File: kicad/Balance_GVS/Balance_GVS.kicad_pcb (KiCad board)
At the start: 2 copper layers, 110 parts, among them J1 Conn_01x02_Pin, J2 USB_C_Receptacle, J3 Conn_01x02_Pin, J4 Conn_01x02_Pin, J5 Conn_01x02_Pin, K1 AQY210S, Q3 2N3904, Q4 2N3904, SW2 EVQ-P7A01P, SW3 SW_Push, SW4 SW_Push, SW5 SW_Push, SW6 SW_Push, SW7 SS-12D00-G 4 E, U1 ESP32-WROOM-32E, U10 INA219BxD, U11 LT1013DIP, U12 LT1013DIP, U3 OPA4313IPWR, U4 INA303A1IPW, U5 TPS7A4901DGNT, U7 MT3608, U8 TP4056, U9 MCP4725xxx-xCH

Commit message: partial non-battery PCB now moved
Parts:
- moved R23 219.6 mm to (265.0, 52.0), turned to -90 degrees
- moved R25 212.7 mm to (254.5, 52.0), turned to 90 degrees
- moved R26 207.1 mm to (249.5, 57.5), turned to 90 degrees
- moved R27 206.3 mm to (258.0, 49.5)
- moved R24 206.3 mm to (256.5, 69.0), turned to -90 degrees
- moved R43 205.9 mm to (250.5, 47.0), turned to -90 degrees
- moved R22 201.5 mm to (252.5, 66.0), turned to 90 degrees
- moved R1 201.2 mm to (252.5, 61.0), turned to -90 degrees
- moved R28 200.8 mm to (254.0, 57.0), turned to 90 degrees
- moved C15 193.1 mm to (265.2, 55.8), turned to 90 degrees
- moved R48 187.9 mm to (248.5, 69.0), turned to 90 degrees
- moved R45 185.2 mm to (235.5, 69.0), turned to 90 degrees
- moved R47 178.0 mm to (239.0, 69.0), turned to 90 degrees
- moved C24 176.5 mm to (247.5, 47.0), turned to 90 degrees
- moved C16 176.5 mm to (261.5, 64.5), turned to -90 degrees
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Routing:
- net 24V: track 0.00 -> 61.8 mm, vias 0 -> 2
- net /HowlandPump/3IN-: track 0.00 -> 46.4 mm, vias 0 -> 2
- net Electrode+: track 0.00 -> 34.2 mm, vias 0 -> 2
- net +3.3V: track 0.00 -> 32.5 mm
- net /Processor/POT_ADC: track 0.00 -> 25.7 mm
- net /HowlandPump/12V: track 0.00 -> 22.0 mm
- net /Processor/EN: track 0.00 -> 21.9 mm
- net /Processor/Button1: track 0.00 -> 20.5 mm
- net /Processor/Switch1: track 0.00 -> 20.2 mm, vias 0 -> 2
- net /Processor/SCL2: track 0.00 -> 19.2 mm, vias 0 -> 2
- net /Processor/SDA2: track 0.00 -> 18.6 mm
- net /Processor/SCL1: track 0.00 -> 16.8 mm, vias 0 -> 2
- net Net-(Q4-B): track 0.00 -> 16.5 mm
- net /Processor/SDA1: track 0.00 -> 15.8 mm
- net Net-(Q3-B): track 0.00 -> 15.4 mm
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
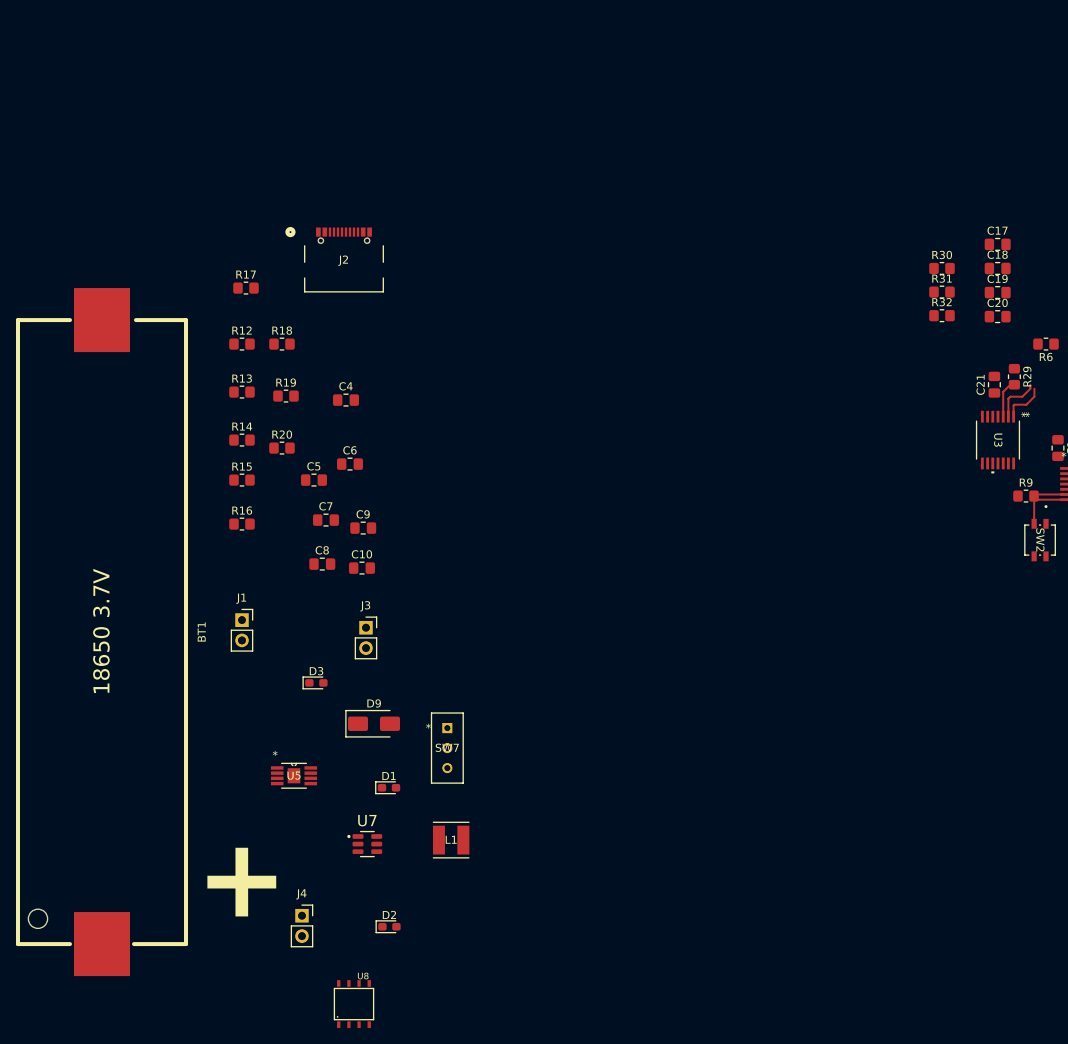
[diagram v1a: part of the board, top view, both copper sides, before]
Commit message: now without battery components in pcb
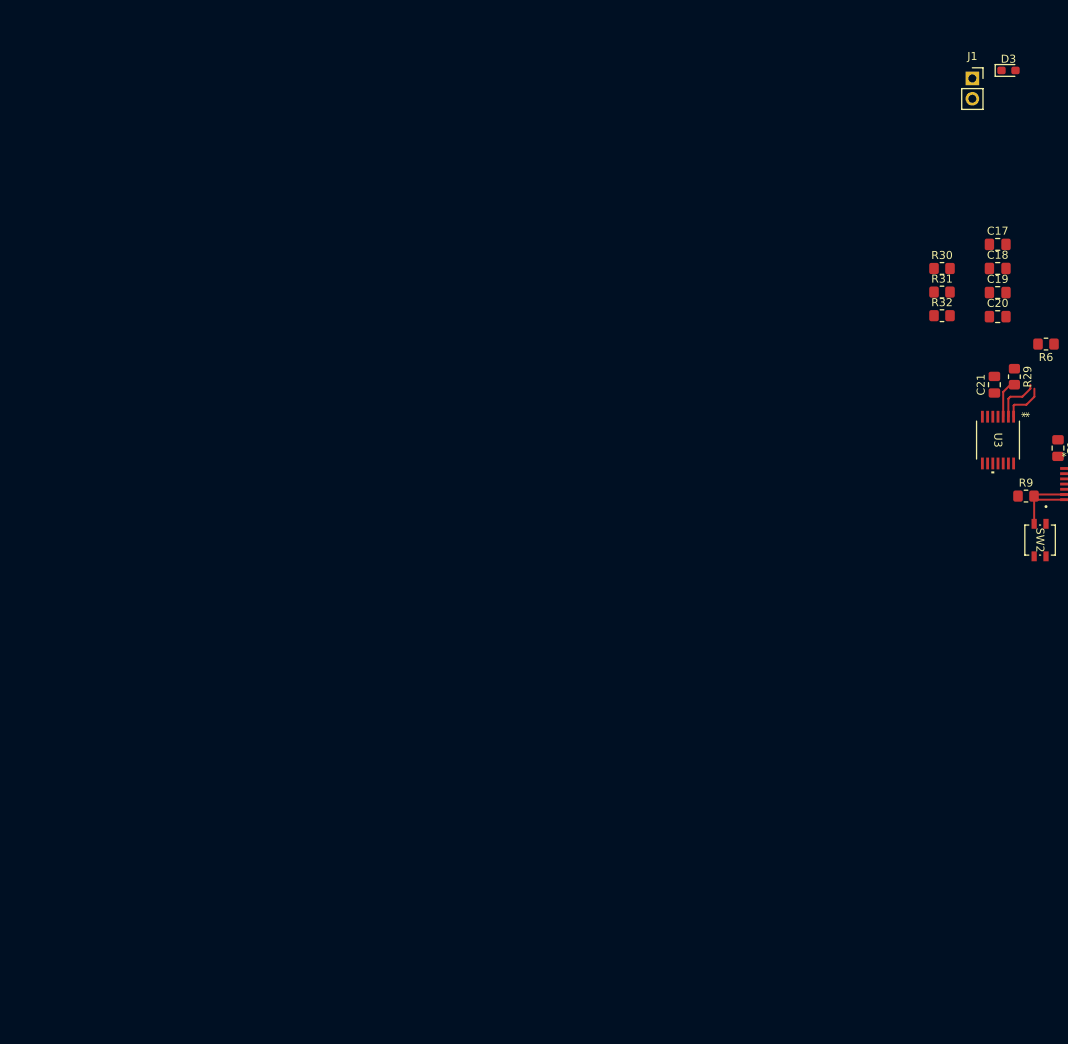
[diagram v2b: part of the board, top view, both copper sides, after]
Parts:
- removed BT1: BK-18650-PC2, FreddyBattery:BH-18650-B1BA002
- removed C10: 2.2µF, Capacitor_SMD:C_0805_2012Metric_Pad1.18x1.45mm_HandSolder
- removed C4, C5, C6, C8, C9: 10µF, Capacitor_SMD:C_0805_2012Metric_Pad1.18x1.45mm_HandSolder
- removed C7: 10nF, Capacitor_SMD:C_0805_2012Metric_Pad1.18x1.45mm_HandSolder
- removed D1, D2: LED_Small, LED_SMD:LED_0603_1608Metric_Pad1.05x0.95mm_HandSolder
- removed D9: SS14, Diode_SMD:D_SMA
- removed J2: USB_C_Receptacle, USB4105_GF_A:USB4105_GCT
- removed J3, J4: Conn_01x02_Pin, Connector_PinSocket_2.54mm:PinSocket_1x02_P2.54mm_Vertical
- removed L1: 4.7µH, SRN4018_4R7M:IND_BOURNS_SRN4018
- removed R12: 191k, Resistor_SMD:R_0805_2012Metric_Pad1.20x1.40mm_HandSolder
- removed R13, R20: 10k, Resistor_SMD:R_0805_2012Metric_Pad1.20x1.40mm_HandSolder
- removed R14: 2.4k, Resistor_SMD:R_0805_2012Metric_Pad1.20x1.40mm_HandSolder
- removed R15, R16: 1k, Resistor_SMD:R_0805_2012Metric_Pad1.20x1.40mm_HandSolder
- removed R17, R18: 5.1k, Resistor_SMD:R_0805_2012Metric_Pad1.20x1.40mm_HandSolder
- removed R19: 412k, Resistor_SMD:R_0805_2012Metric_Pad1.20x1.40mm_HandSolder
- removed SW7: SS-12D00-G 4 E, ul_SS-12D00-G-4-E:1P2T_SS-12D00_CNK
- removed U5: TPS7A4901DGNT, TPS7A4901DGNT _footprints:DGN8_1P89X1P57
- removed U7: MT3608, MT3608:SOT95P280X145-6N
- removed U8: TP4056, TP4056:SOT23-8
- moved D3 115.5 mm to (149.8, 65.3)
- moved J1 113.7 mm to (145.3, 66.3)

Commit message: connected non-battery PCB, with DRC errors
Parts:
- moved R31 122.1 mm to (258.4, 128.0)
- moved R30 119.6 mm to (254.4, 129.7)
- moved C19 113.3 mm to (257.0, 125.5)
- moved R32 110.0 mm to (249.8, 115.1), turned to -90 degrees
- moved C17 109.7 mm to (250.3, 127.7), turned to 180 degrees
- moved C21 108.1 mm to (253.9, 126.5), turned to -90 degrees
- moved C18 107.9 mm to (250.4, 125.2)
- moved C20 106.0 mm to (252.9, 114.0)
- moved U3 105.6 mm to (253.8, 119.6), turned to 90 degrees
- moved R29 103.9 mm to (250.9, 130.7)
- moved D3 98.9 mm to (233.2, 118.5), turned to -90 degrees
- moved R9 95.1 mm to (246.9, 125.1), turned to 90 degrees
- moved J1 91.6 mm to (230.2, 100.7), turned to 90 degrees
- moved SW2 87.1 mm to (240.9, 125.2), turned to 180 degrees
- moved U4 85.4 mm to (245.4, 117.2), turned to 90 degrees
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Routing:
- net 1.65V: track 0.00 -> 43.2 mm, vias 0 -> 4
- net Battery_Voltage: track 4.77 -> 41.7 mm
- net /HowlandPump/2IN+: track 3.08 -> 21.5 mm
- net /Safety/VREF: track 0.00 -> 17.1 mm, vias 0 -> 2
- net Net-(D3-K): track 8.86 -> 24.7 mm
- net /Safety/LIMIT2: track 4.45 -> 17.5 mm
- net /Safety/INP: track 4.44 -> 17.4 mm
- net /HowlandPump/3IN-: track 46.4 -> 36.1 mm
- net 24V: track 61.8 -> 51.5 mm
- net /Safety/0.825V: track 0.00 -> 9.69 mm
- net Electrode+: track 34.2 -> 24.8 mm
- net /Safety/2.475V: track 4.87 -> 12.9 mm
- net +3.3V: track 32.5 -> 35.5 mm
- net Net-(D3-A): track 0.00 -> 2.62 mm
- net /Safety/LIMIT1: track 11.5 -> 13.5 mm, vias 0 -> 2
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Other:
- board outline added: 30 x 100 mm

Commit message: Add shit ton to schematic
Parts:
- added C26: 10nF, Capacitor_SMD:C_0805_2012Metric_Pad1.18x1.45mm_HandSolder, F.Cu at (183.6, 95.2)
- added D10: BAS40, BAS40:P200_SOT-23, F.Cu at (171.3, 77.6)
- added D11: BAS40, BAS40:P200_SOT-23, F.Cu at (171.3, 82.1)
- added D12: BAS40, BAS40:P200_SOT-23, F.Cu at (171.3, 86.5)
- added D13: CMJ3500, Diode_SMD:D_SOD-123F, F.Cu at (182.2, 73.7)
- added D14: CMJ3500, Diode_SMD:D_SOD-123F, F.Cu at (182.2, 77.0)
- added D15: CMJ3500, Diode_SMD:D_SOD-123F, F.Cu at (182.2, 80.4)
- added D4: BAS40, BAS40:P200_SOT-23, F.Cu at (171.3, 73.2)
- added J10: I2C Header 2, Connector_PinSocket_2.54mm:PinSocket_1x02_P2.54mm_Vertical, F.Cu at (176.9, 96.0)
- added J6: Conn_01x03_Pin, Connector_PinHeader_2.54mm:PinHeader_1x03_P2.54mm_Vertical, F.Cu at (181.8, 84.3)
- added J7: Conn_01x03_Pin, Connector_PinHeader_2.54mm:PinHeader_1x03_P2.54mm_Vertical, F.Cu at (186.4, 84.3)
- added J8: Conn_01x05_Pin, Connector_PinSocket_2.54mm:PinSocket_1x05_P2.54mm_Vertical, F.Cu at (177.2, 74.3)
- added J9: I2C Header 1, Connector_PinSocket_2.54mm:PinSocket_1x02_P2.54mm_Vertical, F.Cu at (172.3, 96.0)
- added R52: 10k, Resistor_SMD:R_0805_2012Metric_Pad1.20x1.40mm_HandSolder, F.Cu at (183.6, 98.2)
- R23: value 10K -> 33
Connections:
- K1 pad 4: Electrode- -> Safety+
- R23 pad 1: INA219_IN+ -> Safety-
- R23 pad 2: INA219_IN- -> Current_Sense-
- R39 pad 2: Safety- -> Current_Sense-
- U10 pad 7: INA219_IN- -> Current_Sense-
- U10 pad 8: INA219_IN+ -> Safety-
- U11 pad 3: DAC_OUT -> Net-(U11-1IN_+)
- U12 pad 7: Safety- -> Current_Sense-
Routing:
- net Current_Sense-: track 0.00 -> 6.70 mm
- net INA219_IN+: track 3.53 -> 0.00 mm
- net INA219_IN-: track 2.85 -> 0.00 mm

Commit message: Youssef's change
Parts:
- moved D15 107.7 mm to (280.0, 125.5)
- moved D14 105.9 mm to (279.5, 119.0)
- moved D13 105.0 mm to (279.6, 113.0)
- moved J8 101.0 mm to (278.0, 68.9)
- moved J6 99.5 mm to (280.0, 100.5)
- moved J10 98.3 mm to (272.0, 120.7)
- moved D10 96.2 mm to (267.0, 88.1), turned to 90 degrees
- moved J9 94.7 mm to (264.4, 118.0)
- moved J7 92.2 mm to (278.5, 88.0)
- moved C26 91.3 mm to (274.5, 104.5)
- moved R52 89.5 mm to (272.0, 112.0)
- moved D11 88.6 mm to (259.8, 88.0)
- moved D4 88.3 mm to (259.3, 81.5)
- moved D12 86.7 mm to (257.6, 95.7)
- moved J5 21.4 mm to (276.0, 53.5)
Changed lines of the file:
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@@
 			(net "Net-(Q3-B)")
 			(pinfunction "*ALERT2_11")
-			(pintype "output")
+			(pintype "open_collector")
 		)
 		(pad "12" smd rect
@@
 			(net "Net-(Q3-B)")
 			(pinfunction "*ALERT1_12")
-			(pintype "output")
+			(pintype "open_collector")
 		)
 		(pad "13" smd rect
@@
 	(footprint "BAS40:P200_SOT-23"
 		(layer "F.Cu")
-		(at 171.345 77.645)
+		(at 266.97 88.1 90)
 		(descr "SOT, 3 Pin (https://www.jedec.org/system/files/docs/to-236h.pdf variant AB), generated with kicad-footprint-generator ipc_gullwing_generator.py")
 		(tags "SOT TO_SOT_SMD")
 		(property "Reference" "D10"
-			(at 0.5 -1.25 0)
+			(at 1.2 -1.47 90)
 			(layer "F.SilkS")
 			(effects
@@
 		)
 		(property "Value" "BAS40"
-			(at 1 3.43 0)
+			(at 1 3.43 90)
 			(layer "F.Fab")
 			(effects
@@
 		)
 		(property "Datasheet" "https://diotec.com/de/produktliste/D.html"
-			(at 0 0 0)
+			(at 0 0 90)
 			(layer "F.Fab")
 			(hide yes)
@@
 		)
 		(property "Description" "Diode with NC pin"
-			(at 0 0 0)
+			(at 0 0 90)
 			(layer "F.Fab")
 			(hide yes)
@@
 		(fp_line
 			(start 1.1 -0.62)
-			(end -0.575 -0.62)
+			(end 1.75 -0.62)
 			(stroke
 				(width 0.12)
@@
 		(fp_line
 			(start 1.1 -0.62)
-			(end 1.75 -0.62)
+			(end -0.575 -0.62)
 			(stroke
 				(width 0.12)
@@
 		(fp_line
 			(start 1.1 2.68)
-			(end 0.45 2.68)
+			(end 1.75 2.68)
 			(stroke
 				(width 0.12)
@@
 		(fp_line
 			(start 1.1 2.68)
-			(end 1.75 2.68)
+			(end 0.45 2.68)
 			(stroke
 				(width 0.12)
@@
 		)
 		(fp_line
-			(start -0.82 -0.67)
-			(end -0.82 2.73)
+			(start 3.02 -0.67)
+			(end -0.82 -0.67)
 			(stroke
 				(width 0.05)
@@
 		)
 		(fp_line
-			(start -0.82 2.73)
-			(end 3.02 2.73)
+			(start -0.82 -0.67)
+			(end -0.82 2.73)
 			(stroke
 				(width 0.05)
@@
 		)
 		(fp_line
-			(start 3.02 -0.67)
-			(end -0.82 -0.67)
+			(start 3.02 2.73)
+			(end 3.02 -0.67)
 			(stroke
 				(width 0.05)
@@
 		)
 		(fp_line
-			(start 3.02 2.73)
-			(end 3.02 -0.67)
+			(start -0.82 2.73)
+			(end 3.02 2.73)
 			(stroke
 				(width 0.05)
@@
 		)
 		(fp_line
-			(start 0.45 -0.145)
-			(end 0.775 -0.47)
+			(start 1.75 -0.47)
+			(end 1.75 2.53)
 			(stroke
 				(width 0.1)
@@
 		)
 		(fp_line
-			(start 0.45 2.53)
-			(end 0.45 -0.145)
+			(start 0.775 -0.47)
+			(end 1.75 -0.47)
 			(stroke
 				(width 0.1)
@@
 		)
 		(fp_line
-			(start 0.775 -0.47)
-			(end 1.75 -0.47)
+			(start 0.45 -0.145)
+			(end 0.775 -0.47)
 			(stroke
 				(width 0.1)
@@
 		)
 		(fp_line
-			(start 1.75 -0.47)
-			(end 1.75 2.53)
+			(start 1.75 2.53)
+			(end 0.45 2.53)
 			(stroke
 				(width 0.1)
@@
 		)
 		(fp_line
-			(start 1.75 2.53)
-			(end 0.45 2.53)
+			(start 0.45 2.53)
+			(end 0.45 -0.145)
 			(stroke
 				(width 0.1)
@@
 		)
 		(fp_text user "${REFERENCE}"
-			(at 0.5 -1.25 0)
+			(at 1.2 -1.47 90)
 			(layer "F.Fab")
 			(effects
@@
 		)
 		(pad "1" smd roundrect
-			(at 0 0)
+			(at 0 0 90)
 			(size 1 0.6)
 			(layers "F.Cu" "F.Mask" "F.Paste")
@@
 		)
 		(pad "2" smd roundrect
-			(at 0 2.06)
+			(at 0 2.06 90)
 			(size 1 0.6)
 			(layers "F.Cu" "F.Mask" "F.Paste")
@@
 		)
 		(pad "3" smd roundrect
-			(at 2.2 1.03)
+			(at 2.2 1.03 90)
 			(size 1 0.6)
 			(layers "F.Cu" "F.Mask" "F.Paste")
@@
 		)
 		(embedded_fonts no)
-		(model "${KICAD6_3DMODEL_DIR}/Package_TO_SOT_SMD.3dshapes/SOT-23.wrl"
+		(model "${KICAD10_3DMODEL_DIR}/Package_TO_SOT_SMD.3dshapes/SOT-23.step"
 			(hide yes)
 			(offset
@@
 	(footprint "BAS40:P200_SOT-23"
 		(layer "F.Cu")
-		(at 171.345 73.195)
+		(at 259.3 81.47)
 		(descr "SOT, 3 Pin (https://www.jedec.org/system/files/docs/to-236h.pdf variant AB), generated with kicad-footprint-generator ipc_gullwing_generator.py")
 		(tags "SOT TO_SOT_SMD")
@@
 		)
 		(embedded_fonts no)
-		(model "${KICAD6_3DMODEL_DIR}/Package_TO_SOT_SMD.3dshapes/SOT-23.wrl"
+		(model "${KICAD10_3DMODEL_DIR}/Package_TO_SOT_SMD.3dshapes/SOT-23.step"
 			(hide yes)
 			(offset
@@
 	(footprint "BAS40:P200_SOT-23"
 		(layer "F.Cu")
-		(at 171.345 86.545)
+		(at 257.57 95.7)
 		(descr "SOT, 3 Pin (https://www.jedec.org/system/files/docs/to-236h.pdf variant AB), generated with kicad-footprint-generator ipc_gullwing_generator.py")
 		(tags "SOT TO_SOT_SMD")
@@
 		)
 		(embedded_fonts no)
-		(model "${KICAD6_3DMODEL_DIR}/Package_TO_SOT_SMD.3dshapes/SOT-23.wrl"
+		(model "${KICAD10_3DMODEL_DIR}/Package_TO_SOT_SMD.3dshapes/SOT-23.step"
 			(hide yes)
 			(offset
@@
 	(footprint "Diode_SMD:D_SOD-123F"
 		(layer "F.Cu")
-		(at 182.25 73.675)
+		(at 279.6 113)
 		(descr "D_SOD-123F")
 		(tags "D_SOD-123F")
@@
 	(footprint "Connector_PinSocket_2.54mm:PinSocket_1x02_P2.54mm_Vertical"
 		(layer "F.Cu")
-		(at 176.885 96.015)
+		(at 272 120.73)
 		(descr "Through hole straight socket strip, 1x02, 2.54mm pitch, single row (from Kicad 4.0.7), script generated")
 		(tags "Through hole socket strip THT 1x02 2.54mm single row")
@@
 	(footprint "Connector_PinSocket_2.54mm:PinSocket_1x02_P2.54mm_Vertical"
 		(layer "F.Cu")
-		(at 172.295 96.015)
+		(at 264.41 117.96)
 		(descr "Through hole straight socket strip, 1x02, 2.54mm pitch, single row (from Kicad 4.0.7), script generated")
 		(tags "Through hole socket strip THT 1x02 2.54mm single row")
@@
 	(footprint "Connector_PinHeader_2.54mm:PinHeader_1x03_P2.54mm_Vertical"
 		(layer "F.Cu")
-		(at 186.365 84.345)
+		(at 278.5 88)
 		(descr "Through hole straight pin header, 1x03, 2.54mm pitch, single row")
 		(tags "Through hole pin header THT 1x03 2.54mm single row")
@@
 	(footprint "BAS40:P200_SOT-23"
 		(layer "F.Cu")
-		(at 171.345 82.095)
+		(at 259.8 87.97)
 		(descr "SOT, 3 Pin (https://www.jedec.org/system/files/docs/to-236h.pdf variant AB), generated with kicad-footprint-generator ipc_gullwing_generator.py")
 		(tags "SOT TO_SOT_SMD")
@@
 		)
 		(embedded_fonts no)
-		(model "${KICAD6_3DMODEL_DIR}/Package_TO_SOT_SMD.3dshapes/SOT-23.wrl"
+		(model "${KICAD10_3DMODEL_DIR}/Package_TO_SOT_SMD.3dshapes/SOT-23.step"
 			(hide yes)
 			(offset
@@
 	(footprint "Connector_PinSocket_2.54mm:PinSocket_1x05_P2.54mm_Vertical"
 		(layer "F.Cu")
-		(at 177.185 74.295)
+		(at 278 68.88)
 		(descr "Through hole straight socket strip, 1x05, 2.54mm pitch, single row (from Kicad 4.0.7), script generated")
 		(tags "Through hole socket strip THT 1x05 2.54mm single row")
@@
 		)
 		(property "Value" "Conn_01x05_Pin"
-			(at 0 12.93 0)
+			(at 11.5 48.93 0)
 			(layer "F.Fab")
 			(effects
@@
 	(footprint "Connector_PinSocket_2.54mm:PinSocket_1x02_P2.54mm_Vertical"
 		(layer "F.Cu")
-		(at 268.5 73.5)
+		(at 276 53.5)
 		(descr "Through hole straight socket strip, 1x02, 2.54mm pitch, single row (from Kicad 4.0.7), script generated")
 		(tags "Through hole socket strip THT 1x02 2.54mm single row")
@@
 	(footprint "Diode_SMD:D_SOD-123F"
 		(layer "F.Cu")
-		(at 182.25 77.025)
+		(at 279.5 119)
 		(descr "D_SOD-123F")
 		(tags "D_SOD-123F")
@@
 	(footprint "Resistor_SMD:R_0805_2012Metric_Pad1.20x1.40mm_HandSolder"
 		(layer "F.Cu")
-		(at 183.555 98.205)
+		(at 272 112)
 		(descr "Resistor SMD 0805 (2012 Metric), square (rectangular) end terminal, IPC-7351 nominal with elongated pad for handsoldering. (Body size source: IPC-SM-782 page 72, https://www.pcb-3d.com/wordpress/wp-content/uploads/ipc-sm-782a_amendment_1_and_2.pdf)")
 		(tags "resistor handsolder")
@@
 	(footprint "Capacitor_SMD:C_0805_2012Metric_Pad1.18x1.45mm_HandSolder"
 		(layer "F.Cu")
-		(at 183.585 95.225)
+		(at 274.4625 104.5)
 		(descr "Capacitor SMD 0805 (2012 Metric), square (rectangular) end terminal, IPC-7351 nominal with elongated pad for handsoldering. (Body size source: IPC-SM-782 page 76, https://www.pcb-3d.com/wordpress/wp-content/uploads/ipc-sm-782a_amendment_1_and_2.pdf, https://docs.google.com/spreadsheets/d/1BsfQQcO9C6DZCsRaXUlFlo91Tg2WpOkGARC1WS5S8t0/edit?usp=sharing)")
 		(tags "capacitor handsolder")
@@
 	(footprint "Connector_PinHeader_2.54mm:PinHeader_1x03_P2.54mm_Vertical"
 		(layer "F.Cu")
-		(at 181.775 84.345)
+		(at 280 100.46)
 		(descr "Through hole straight pin header, 1x03, 2.54mm pitch, single row")
 		(tags "Through hole pin header THT 1x03 2.54mm single row")
@@
 	(footprint "Diode_SMD:D_SOD-123F"
 		(layer "F.Cu")
-		(at 182.25 80.375)
+		(at 279.975 125.53)
 		(descr "D_SOD-123F")
 		(tags "D_SOD-123F")
@@
 	)
 	(segment
+		(start 239.76 141.5)
+		(end 240.53 142.27)
+		(width 0.25)
+		(layer "F.Cu")
+		(net "Current_Sense-")
+	)
+	(segment
+		(start 262.225 53.185)
+		(end 264.815 53.185)
+		(width 0.2)
+		(layer "F.Cu")
+		(net "Current_Sense-")
+	)
+	(segment
+		(start 264.815 53.185)
+		(end 265 53)
+		(width 0.2)
+		(layer "F.Cu")
+		(net "Current_Sense-")
+	)
+	(segment
+		(start 237 141.5)
+		(end 239.76 141.5)
+		(width 0.25)
+		(layer "F.Cu")
+		(net "Current_Sense-")
+	)
+	(segment
 		(start 248 57.5)
 		(end 248 60.5)
@@
 		(net "Net-(U11-2OUT)")
 	)
-	(segment
-		(start 239.76 141.5)
-		(end 240.53 142.27)
-		(width 0.25)
-		(layer "F.Cu")
-		(net "Current_Sense-")
-	)
-	(segment
-		(start 262.225 53.185)
-		(end 264.815 53.185)
-		(width 0.2)
-		(layer "F.Cu")
-		(net "Current_Sense-")
-	)
-	(segment
-		(start 264.815 53.185)
-		(end 265 53)
-		(width 0.2)
-		(layer "F.Cu")
-		(net "Current_Sense-")
-	)
-	(segment
-		(start 237 141.5)
-		(end 239.76 141.5)
-		(width 0.25)
-		(layer "F.Cu")
-		(net "Current_Sense-")
-	)
 	(embedded_fonts no)

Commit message: adding CLDs in progress
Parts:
- moved J9 80.5 mm to (184.0, 121.5)
- moved J10 80.5 mm to (191.6, 124.3)
- moved J8 73.2 mm to (217.0, 109.4)
- moved D15 44.5 mm to (264.0, 84.0)
- moved D14 41.6 mm to (257.0, 84.0), turned to 180 degrees
- moved J6 35.1 mm to (249.0, 84.0)
- moved R52 33.8 mm to (276.5, 145.5)
- moved C26 30.8 mm to (267.5, 134.5)
- moved D13 30.4 mm to (255.1, 95.0)
- moved J7 16.0 mm to (265.0, 96.5), turned to 180 degrees
- moved D11 12.9 mm to (251.1, 97.6), turned to 180 degrees
- moved D4 10.3 mm to (255.4, 91.0), turned to 90 degrees
- moved D10 10.2 mm to (261.1, 96.5), turned to 180 degrees
- moved D12 6.84 mm to (253.9, 101.5), turned to 90 degrees
- moved R7 2.03 mm to (265.4, 129.0)
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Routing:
- net Net-(D10-A): track 0.00 -> 13.6 mm
- net Net-(D10-C): track 0.00 -> 13.5 mm
- net Net-(D11-A): track 0.00 -> 11.6 mm
- net /HowlandPump/1IN-: track 11.7 -> 0.21 mm
- net Net-(D11-C): track 0.00 -> 7.64 mm
- net /HowlandPump/2IN+: track 21.5 -> 14.0 mm
- net 1.65V: track 43.2 -> 38.5 mm, vias 4 -> 2
- net Net-(D14-K): track 0.00 -> 4.20 mm
- net DAC_OUT: track 3.58 -> 0.00 mm
